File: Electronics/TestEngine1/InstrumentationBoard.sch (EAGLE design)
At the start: 106 parts, among them IC1 MAX31855, J1 1X2-3.5MM, Q1 MOSFET-NCHANNELBSS123LT1G, Q2 MOSFET-NCHANNELBSS123LT1G, Q3 MOSFET-NCHANNELBSS123LT1G, U1 BMP180

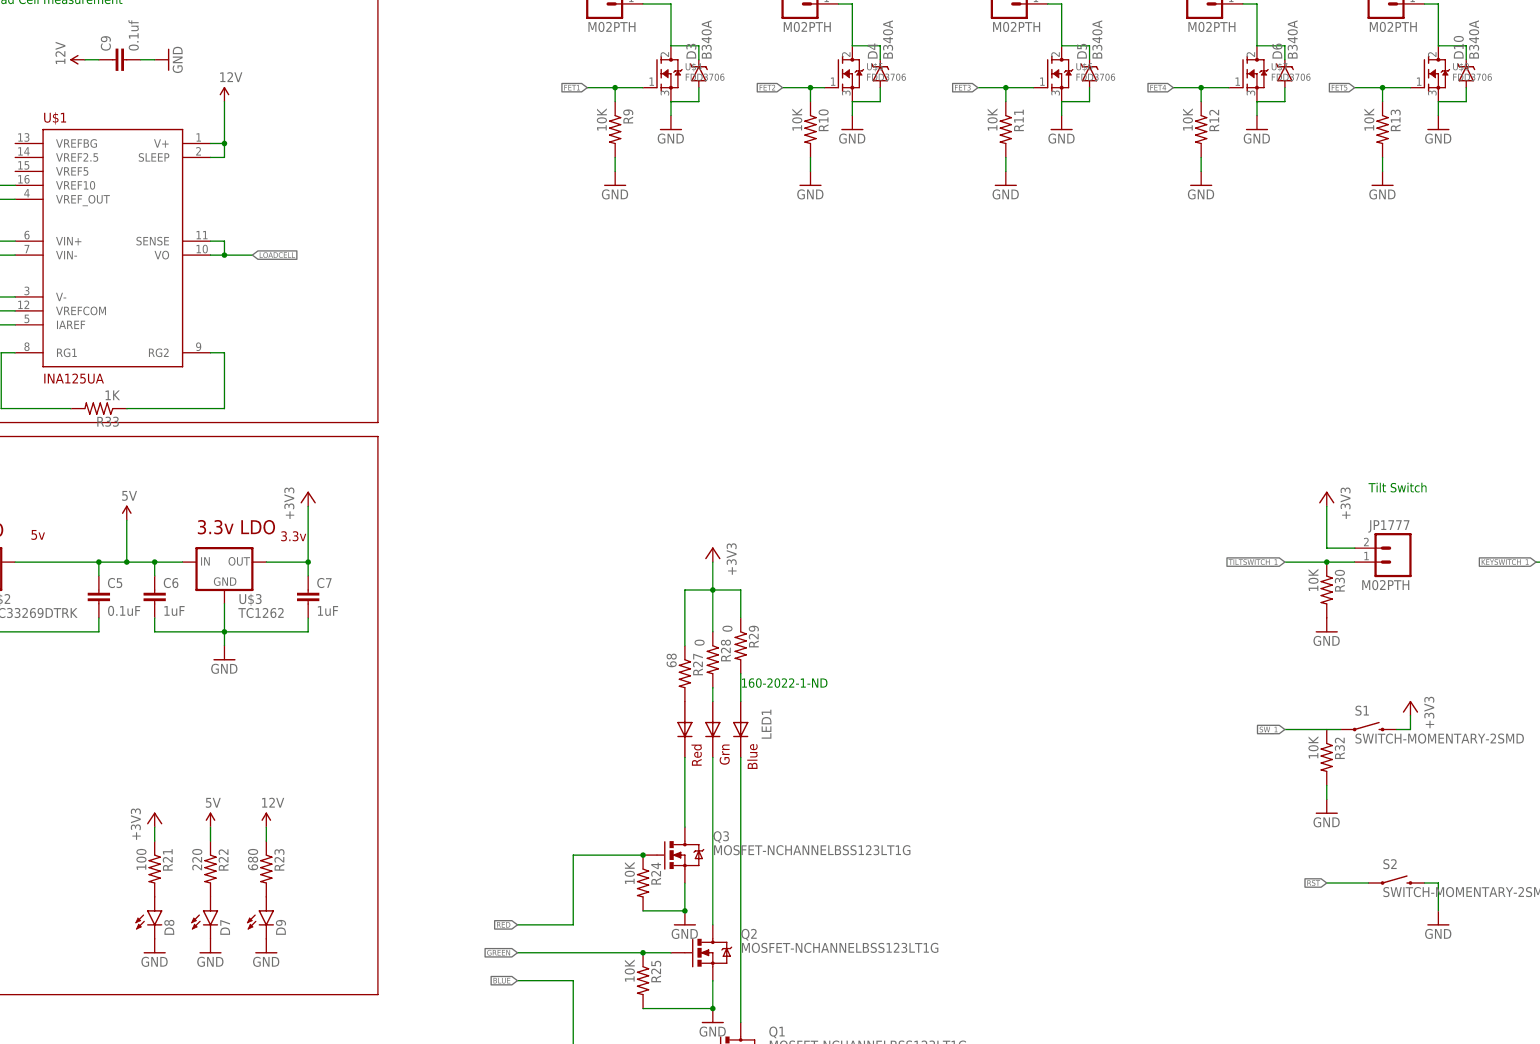
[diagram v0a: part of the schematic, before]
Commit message: added silkscreen moved things around
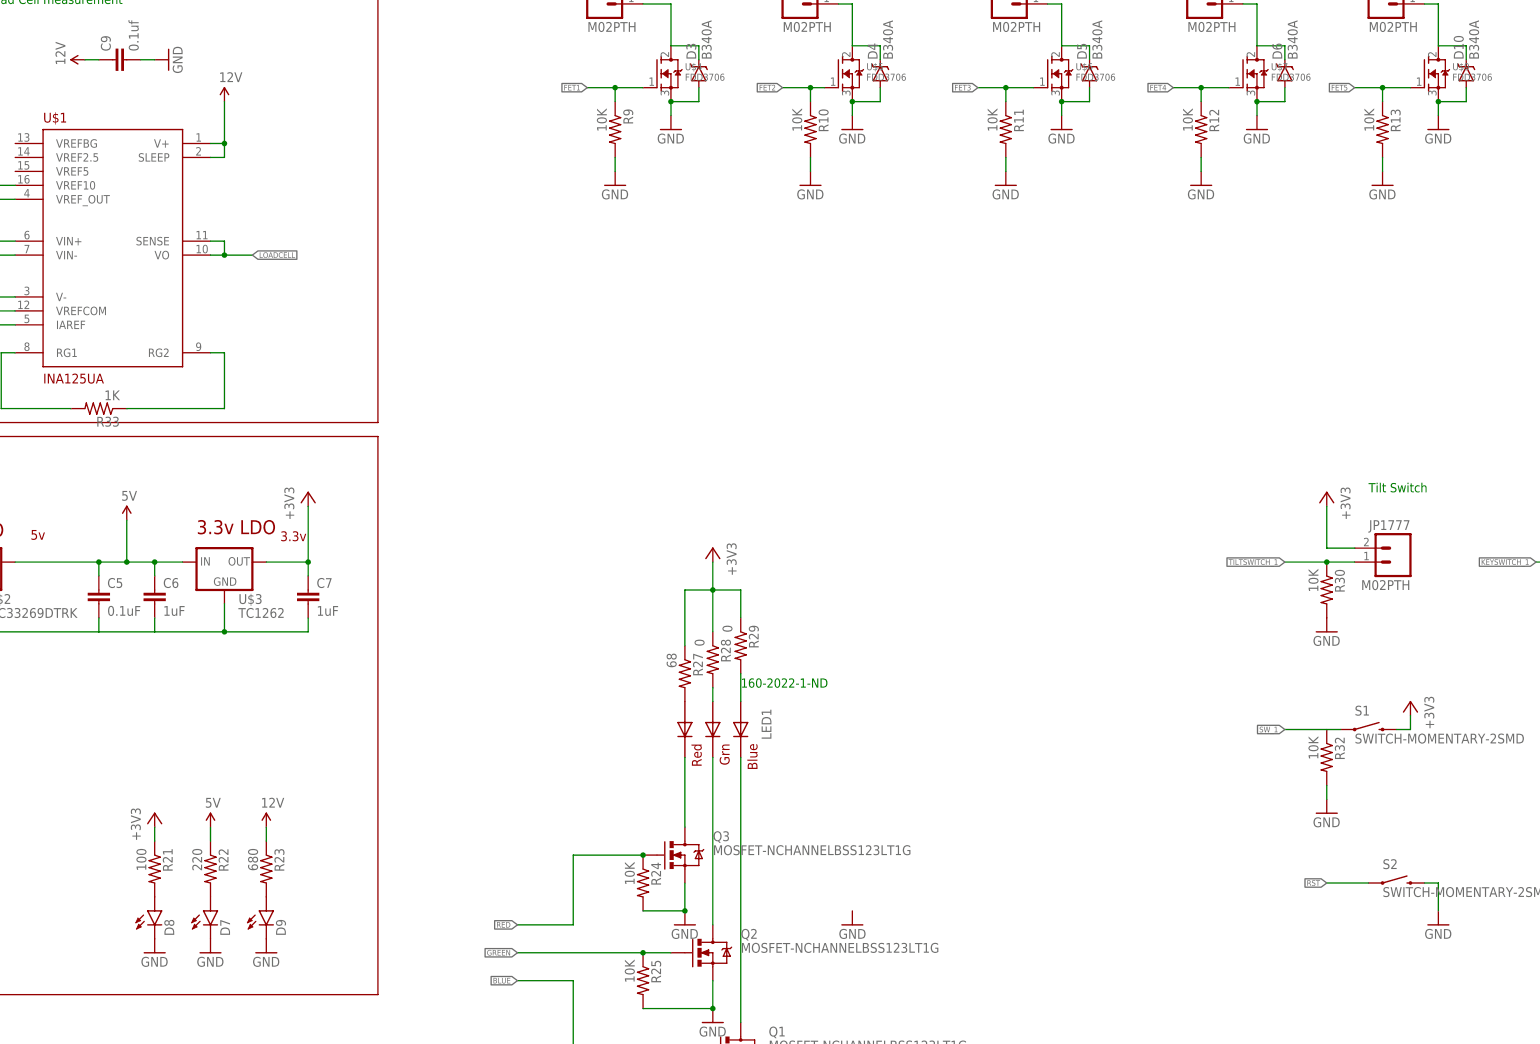
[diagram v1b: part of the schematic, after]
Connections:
- net N$1 renamed TT+
- net N$11 renamed VIN-
- net N$16 renamed VIN+
- net N$20 renamed EXCITE+
- net N$4 renamed T+
- net N$5 renamed TT-
- net N$6 renamed T-
- removed net N$12: C4.2, C5.2, J3.1, U$2.GND
- net GND: now also C4.2, C5.2, J3.1, U$2.GND
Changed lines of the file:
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@@
 <part name="U$2" library="RitLaunchInitiative" deviceset="MC33269DTRK" device=""/>
 <part name="U$3" library="RitLaunchInitiative" deviceset="TC1262" device=""/>
-<part name="GND8" library="supply1" deviceset="GND" device=""/>
-<part name="GND9" library="supply1" deviceset="GND" device=""/>
+<part name="GND" library="supply1" deviceset="GND" device=""/>
 <part name="SUPPLY1" library="SparkFun-Aesthetics" deviceset="5V" device=""/>
 <part name="C4" library="SparkFun-Capacitors" deviceset="CAP" device="0805" value="0.33uF"/>
@@
 <part name="S2" library="SparkFun-Electromechanical" deviceset="SWITCH-MOMENTARY-2" device="SMD"/>
 <part name="GND60" library="supply1" deviceset="GND" device=""/>
+<part name="GND8" library="supply1" deviceset="GND" device=""/>
 </parts>
 <sheets>
@@
 <instance part="U$2" gate="G$1" x="-101.6" y="-5.08"/>
 <instance part="U$3" gate="G$1" x="-55.88" y="-7.62"/>
-<instance part="GND8" gate="1" x="-101.6" y="-22.86"/>
-<instance part="GND9" gate="1" x="-55.88" y="-22.86"/>
+<instance part="GND" gate="1" x="-101.6" y="-22.86"/>
 <instance part="SUPPLY1" gate="G$1" x="-73.66" y="2.54"/>
 <instance part="C4" gate="G$1" x="-114.3" y="-12.7"/>
@@
 <instance part="S2" gate="G$1" x="157.48" y="-63.5"/>
 <instance part="GND60" gate="1" x="165.1" y="-71.12"/>
+<instance part="GND8" gate="1" x="58.42" y="-71.12" rot="MR0"/>
 </instances>
 <busses>
@@
 <pinref part="GND3" gate="1" pin="GND"/>
 <wire x1="213.36" y1="137.16" x2="213.36" y2="134.62" width="0.1524" layer="91"/>
-</segment>
-<segment>
-<pinref part="GND9" gate="1" pin="GND"/>
-<wire x1="-55.88" y1="-12.7" x2="-55.88" y2="-17.78" width="0.1524" layer="91"/>
-<pinref part="C6" gate="G$1" pin="2"/>
-<wire x1="-55.88" y1="-17.78" x2="-55.88" y2="-20.32" width="0.1524" layer="91"/>
-<wire x1="-68.58" y1="-15.24" x2="-68.58" y2="-17.78" width="0.1524" layer="91"/>
-<wire x1="-68.58" y1="-17.78" x2="-55.88" y2="-17.78" width="0.1524" layer="91"/>
-<pinref part="C7" gate="G$1" pin="2"/>
-<wire x1="-40.64" y1="-15.24" x2="-40.64" y2="-17.78" width="0.1524" layer="91"/>
-<wire x1="-40.64" y1="-17.78" x2="-55.88" y2="-17.78" width="0.1524" layer="91"/>
-<pinref part="U$3" gate="G$1" pin="GND"/>
-<junction x="-55.88" y="-17.78"/>
 </segment>
 <segment>
@@
 <wire x1="101.6" y1="78.74" x2="96.52" y2="78.74" width="0.1524" layer="91"/>
 <pinref part="D5" gate="G$1" pin="A"/>
+<junction x="96.52" y="78.74"/>
 </segment>
 <segment>
@@
 <wire x1="63.5" y1="78.74" x2="58.42" y2="78.74" width="0.1524" layer="91"/>
 <pinref part="D4" gate="G$1" pin="A"/>
+<junction x="58.42" y="78.74"/>
 </segment>
 <segment>
@@
 <wire x1="30.48" y1="81.28" x2="30.48" y2="78.74" width="0.1524" layer="91"/>
 <wire x1="30.48" y1="78.74" x2="25.4" y2="78.74" width="0.1524" layer="91"/>
+<junction x="25.4" y="78.74"/>
 </segment>
 <segment>
@@
 <wire x1="137.16" y1="78.74" x2="132.08" y2="78.74" width="0.1524" layer="91"/>
 <pinref part="D6" gate="G$1" pin="A"/>
+<junction x="132.08" y="78.74"/>
 </segment>
 <segment>
@@
 <wire x1="170.18" y1="78.74" x2="165.1" y2="78.74" width="0.1524" layer="91"/>
 <pinref part="D10" gate="G$1" pin="A"/>
+<junction x="165.1" y="78.74"/>
 </segment>
 <segment>
@@
 <wire x1="162.56" y1="-63.5" x2="165.1" y2="-63.5" width="0.1524" layer="91"/>
 <wire x1="165.1" y1="-63.5" x2="165.1" y2="-68.58" width="0.1524" layer="91"/>
+</segment>
+<segment>
+<pinref part="U$2" gate="G$1" pin="GND"/>
+<wire x1="-101.6" y1="-12.7" x2="-101.6" y2="-17.78" width="0.1524" layer="91"/>
+<pinref part="GND" gate="1" pin="GND"/>
+<pinref part="J3" gate="G$1" pin="1"/>
+<wire x1="-101.6" y1="-17.78" x2="-101.6" y2="-20.32" width="0.1524" layer="91"/>
+<wire x1="-124.46" y1="-17.78" x2="-114.3" y2="-17.78" width="0.1524" layer="91"/>
+<pinref part="C4" gate="G$1" pin="2"/>
+<wire x1="-114.3" y1="-17.78" x2="-101.6" y2="-17.78" width="0.1524" layer="91"/>
+<wire x1="-114.3" y1="-15.24" x2="-114.3" y2="-17.78" width="0.1524" layer="91"/>
+<pinref part="C5" gate="G$1" pin="2"/>
+<wire x1="-101.6" y1="-17.78" x2="-78.74" y2="-17.78" width="0.1524" layer="91"/>
+<wire x1="-78.74" y1="-17.78" x2="-78.74" y2="-15.24" width="0.1524" layer="91"/>
+<junction x="-114.3" y="-17.78"/>
+<junction x="-101.6" y="-17.78"/>
+<wire x1="-55.88" y1="-12.7" x2="-55.88" y2="-17.78" width="0.1524" layer="91"/>
+<pinref part="C6" gate="G$1" pin="2"/>
+<wire x1="-68.58" y1="-15.24" x2="-68.58" y2="-17.78" width="0.1524" layer="91"/>
+<wire x1="-68.58" y1="-17.78" x2="-55.88" y2="-17.78" width="0.1524" layer="91"/>
+<pinref part="C7" gate="G$1" pin="2"/>
+<wire x1="-40.64" y1="-15.24" x2="-40.64" y2="-17.78" width="0.1524" layer="91"/>
+<wire x1="-40.64" y1="-17.78" x2="-55.88" y2="-17.78" width="0.1524" layer="91"/>
+<pinref part="U$3" gate="G$1" pin="GND"/>
+<junction x="-55.88" y="-17.78"/>
+<wire x1="-68.58" y1="-17.78" x2="-78.74" y2="-17.78" width="0.1524" layer="91"/>
 </segment>
 </net>
@@
 </segment>
 </net>
-<net name="N$1" class="0">
+<net name="TT+" class="0">
 <segment>
 <wire x1="-132.08" y1="132.08" x2="-132.08" y2="137.16" width="0.1524" layer="91"/>
@@
 </segment>
 </net>
-<net name="N$4" class="0">
+<net name="T+" class="0">
 <segment>
 <pinref part="FB1" gate="G$1" pin="P$2"/>
@@
 </segment>
 </net>
-<net name="N$5" class="0">
+<net name="TT-" class="0">
 <segment>
 <wire x1="-132.08" y1="129.54" x2="-132.08" y2="124.46" width="0.1524" layer="91"/>
@@
 </segment>
 </net>
-<net name="N$6" class="0">
+<net name="T-" class="0">
 <segment>
 <pinref part="FB2" gate="G$1" pin="P$2"/>
@@
 <pinref part="U$10" gate="G$1" pin="AIN3/PE0"/>
 <wire x1="-142.24" y1="264.16" x2="-121.92" y2="264.16" width="0.1524" layer="91"/>
-</segment>
-</net>
-<net name="N$12" class="0">
-<segment>
-<pinref part="U$2" gate="G$1" pin="GND"/>
-<wire x1="-101.6" y1="-12.7" x2="-101.6" y2="-17.78" width="0.1524" layer="91"/>
-<pinref part="GND8" gate="1" pin="GND"/>
-<pinref part="J3" gate="G$1" pin="1"/>
-<wire x1="-101.6" y1="-17.78" x2="-101.6" y2="-20.32" width="0.1524" layer="91"/>
-<wire x1="-124.46" y1="-17.78" x2="-114.3" y2="-17.78" width="0.1524" layer="91"/>
-<pinref part="C4" gate="G$1" pin="2"/>
-<wire x1="-114.3" y1="-17.78" x2="-101.6" y2="-17.78" width="0.1524" layer="91"/>
-<wire x1="-114.3" y1="-15.24" x2="-114.3" y2="-17.78" width="0.1524" layer="91"/>
-<pinref part="C5" gate="G$1" pin="2"/>
-<wire x1="-101.6" y1="-17.78" x2="-78.74" y2="-17.78" width="0.1524" layer="91"/>
-<wire x1="-78.74" y1="-17.78" x2="-78.74" y2="-15.24" width="0.1524" layer="91"/>
-<junction x="-114.3" y="-17.78"/>
-<junction x="-101.6" y="-17.78"/>
 </segment>
 </net>
@@
 </segment>
 </net>
-<net name="N$11" class="0">
+<net name="VIN-" class="0">
 <segment>
 <pinref part="U$1" gate="G$1" pin="VIN-"/>
@@
 </segment>
 </net>
-<net name="N$16" class="0">
+<net name="VIN+" class="0">
 <segment>
 <pinref part="U$1" gate="G$1" pin="VIN+"/>
@@
 </segment>
 </net>
-<net name="N$20" class="0">
+<net name="EXCITE+" class="0">
 <segment>
 <wire x1="-99.06" y1="63.5" x2="-99.06" y2="60.96" width="0.1524" layer="91"/>

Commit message: changed some minor component values and added part numbers
added attributes to parts for digikey part numbers and changed some
values to match whats available on the market
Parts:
- C3: DIGIKEY (none) -> 490-1664-1-ND
- D7, D8, D9: DIGIKEY 350-2048-1-ND -> 160-1405-1-ND
- FB1, FB2: DIGIKEY (none) -> 732-1609-1-ND
- LED1: DIGIKEY (none) -> 1516-1131-1-ND
- R14, R16, R18: value 1.7k -> 1.8k; DIGIKEY (none) -> RMCF0805FT1K80CT-ND
- R15, R17, R36: DIGIKEY (none) -> RHM3.30KCHCT-ND
- R19: value 9k -> 3k
- R20: value 3k -> 1k
- R21: value 100 -> 226; DIGIKEY (none) -> P226CCT-ND
- R22: value 220 -> 560; DIGIKEY (none) -> P560CCT-ND
- R23: value 680 -> 2k; DIGIKEY (none) -> P2.00KCCT-ND
- U$2: DIGIKEY (none) -> MC33269DTRK-5.0GOSCT-ND
- U$3: DIGIKEY (none) -> TC1262-3.3VDBCT-ND
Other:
- note removed: "160-2022-1-ND"
- moved on the sheet: C13, C14, R29
